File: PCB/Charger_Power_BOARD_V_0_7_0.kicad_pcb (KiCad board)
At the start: 4 copper layers, 208 x 117.5 mm, 333 parts, among them IC10 TLA431AIDBZR, IC15 VO618A-3X017T, IC16 LM4040C30FTA, IC17 MCP6541RT-I_OT, IC18 VO618A-3X017T, IC19 TPS54302DDCT, IC20 74LVC1G17GW,125, IC21 VO618A-3X017T, IC22 LM4040C30FTA, IC23 MCP6541RT-I_OT, IC24 VO618A-3X017T, IC25 74LVC1G17GW,125, IC26 VO618A-3X017T, IC27 LM4040C30FTA, IC28 LM75BD,118, IC45 MCP6541RT-I_OT, IC46 VO618A-3X017T, IC47 74LVC1G17GW,125, IC48 VO618A-3X017T, IC49 LM4040C30FTA, IC50 MCP6541RT-I_OT, IC51 VO618A-3X017T, IC52 74LVC1G17GW,125, IC9 STM32C031C6T6, J1 AMT0440005TH0000G, J10 AMT0440005TH0000G, J11 AMT0440005TH0000G, J12 AMT0440005TH0000G, J13 AMT0440005TH0000G, J14 AMT0440005TH0000G, J15 AMT0440005TH0000G, J18 Conn_01x03_Pin, J19 Screw_Terminal_01x02, J2 Conn_01x05_Socket, J20 Screw_Terminal_01x02, J3 AMT0440005TH0000G, J4 Conn_01x04_Socket, J5 AMT0440005TH0000G, J6 B6B-XH-A_LF__SN_, J7 AMT0440005TH0000G, J8 Conn_01x02_Socket, J9 B6B-XH-A_LF__SN_, K5 Relay_IM_NE801A, K6 Relay_IM_NE801A, Q10 DMN60H080DS, Q5 BSS316N H6327, Q6 BSS316N H6327, Q7 DMN60H080DS, Q8 DMN60H080DS, Q9 DMN60H080DS, SW1 SW_SPST, SW2 SW_SPST, T11 ZMPT101B, T7 ZMPT101B, T9 ZMPT101B, U1 THVD1400DR, U10 IVY-CT-PCB-01-10A, U11 DRV8220DRL, U12 IVY-CT-PCB-01-10A, U13 IVY-CT-PCB-01-10A, U4 TLV1805DBVR, U5 TLV1805DBVR, U6 ADE7953xCP, U7 ADE7953xCP, U8 RCD MD0630STA-P, U9 ADE7953xCP, Y3 CX2016FB48000C0FZZH1, Y4 GC0350016, Y5 GC0350016, Y6 GC0350016

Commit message: continuação do layout
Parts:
- moved C29 125.5 mm to (112.2, -16.5)
- moved C30 125.5 mm to (112.2, -14.0)
- moved IC20 125.5 mm to (122.9, -34.3)
- moved R74 125.5 mm to (120.2, -21.5)
- moved R75 125.5 mm to (120.2, -19.0)
- moved D28 102.1 mm to (201.5, 38.0)
- moved R73 95.9 mm to (187.8, 31.5), turned to 180 degrees
- moved R49 95.8 mm to (187.8, 34.0), turned to 180 degrees
- moved C25 92.8 mm to (190.2, 34.5), turned to -90 degrees
- moved R50 89.3 mm to (197.0, 34.5), turned to 90 degrees
- moved C27 86.8 mm to (198.5, 34.5), turned to 90 degrees
- moved IC16 86.7 mm to (193.2, 34.5)
- moved IC17 86.6 mm to (193.2, 29.5)
- moved R66 84.6 mm to (204.5, 35.5)
- moved R70 84.4 mm to (190.2, 29.5), turned to -90 degrees
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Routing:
- net -12V: track 50.6 -> 57.8 mm, vias 4 -> 5
- net +3V3: track 89.0 -> 81.8 mm, vias 27 -> 26
- net /UART0_RX: track 75.3 -> 72.4 mm, vias 2 -> 1
- net /UART0_TX: track 75.5 -> 74.2 mm, vias 2 -> 1
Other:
- outline, holes or cut-outs redrawn

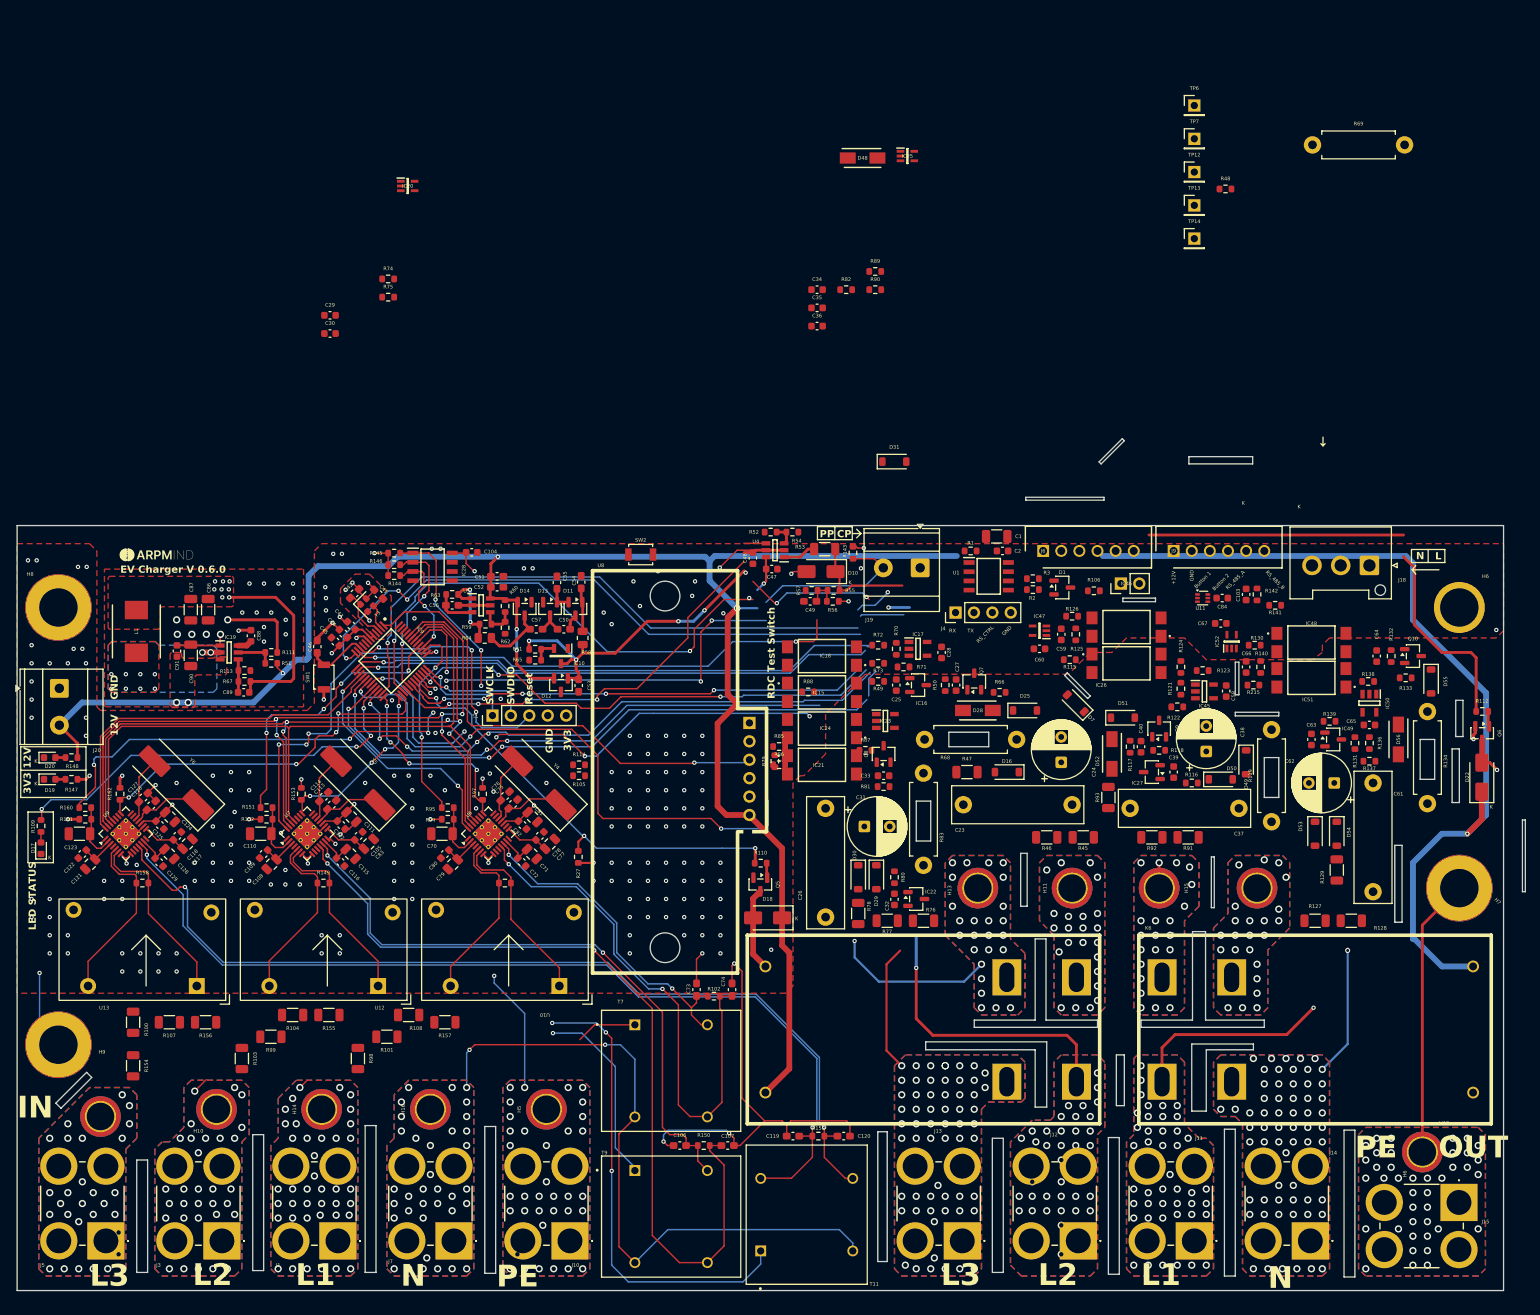
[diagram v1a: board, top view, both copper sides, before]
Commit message: Routing terminado; A corrigir violações; falta colocar as proteçãoes de inversão de polaridade; fusivél; TVS
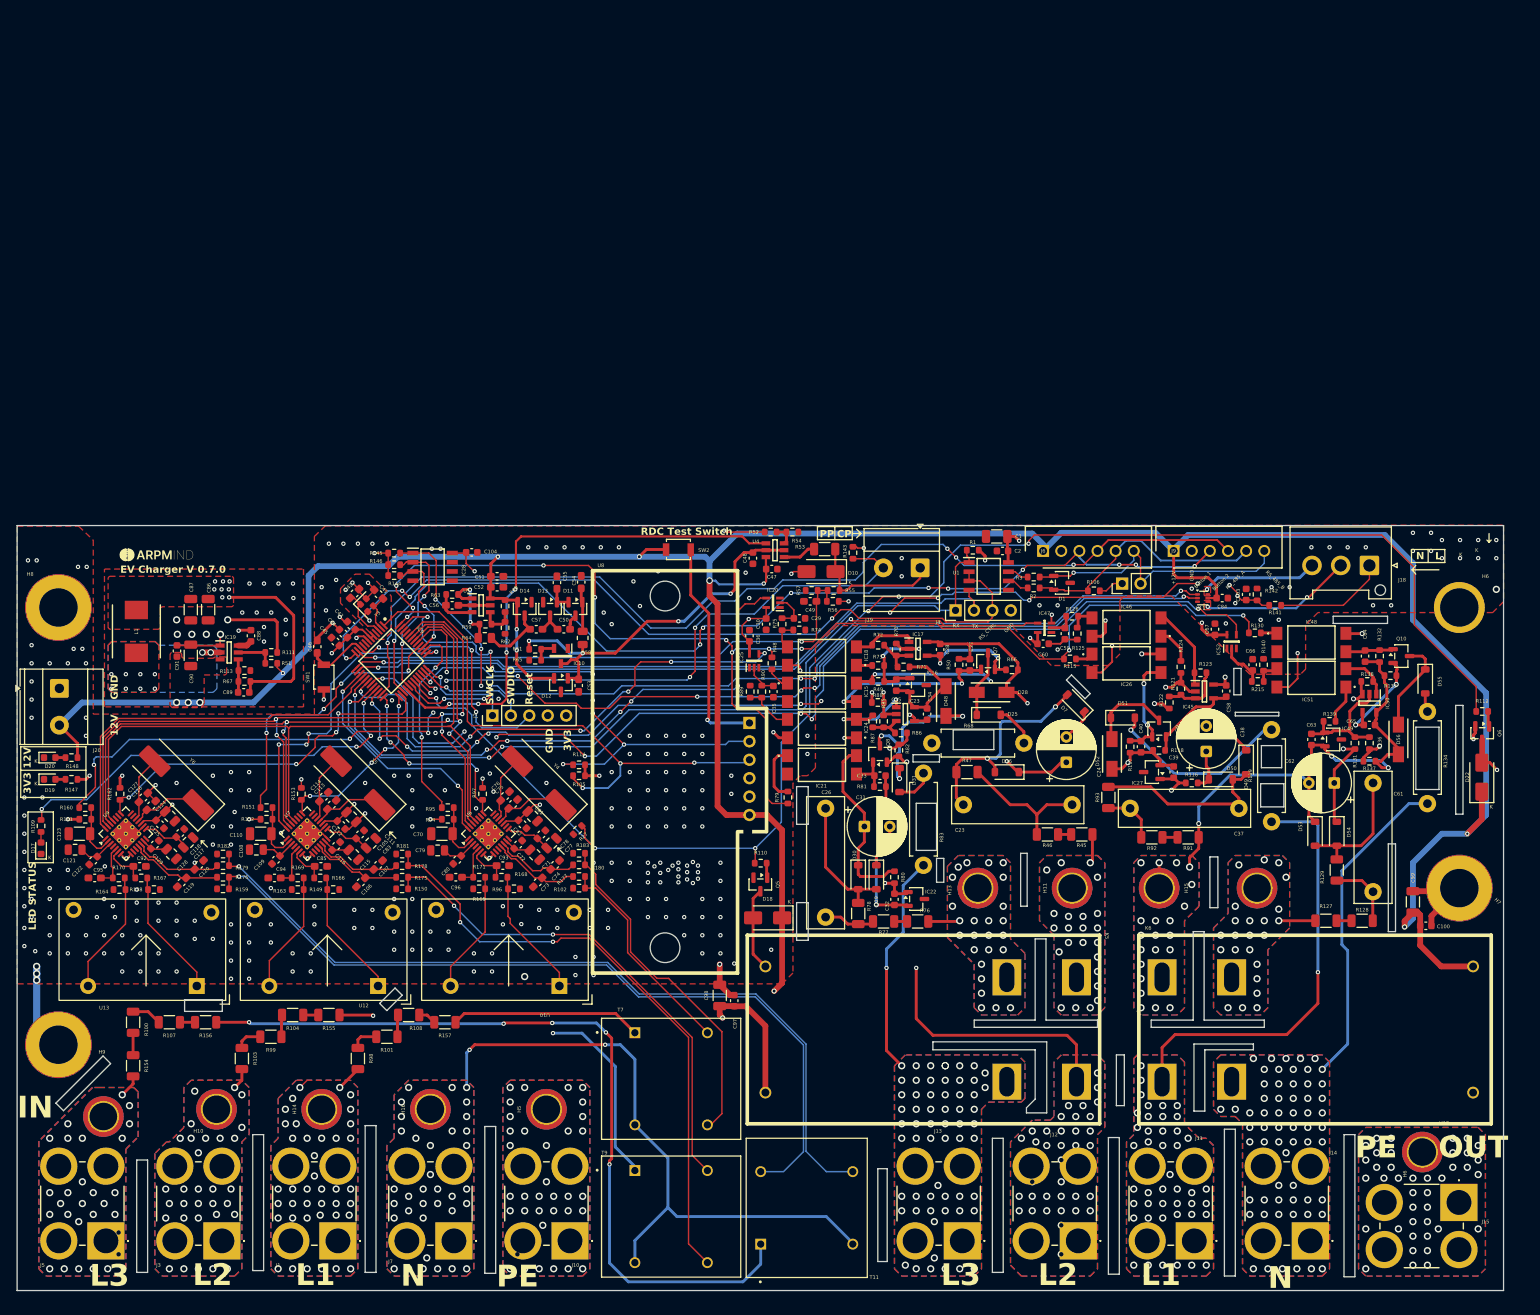
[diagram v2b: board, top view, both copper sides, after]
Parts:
- removed R69: 22K, Resistor_THT:R_Axial_DIN0411_L9.9mm_D3.6mm_P12.70mm_Horizontal
- removed TP12, TP13, TP14, TP6, TP7: TestPoint, Connector_PinHeader_2.54mm:PinHeader_1x01_P2.54mm_Vertical
- added C100: 0.1uF, Capacitor_SMD:C_0603_1608Metric, F.Cu at (263.3, 67.7)
- added C85: 33nF, Capacitor_SMD:C_0603_1608Metric_Pad1.08x0.95mm_HandSolder, F.Cu at (110.9, 59.5)
- added C92: 33nF, Capacitor_SMD:C_0603_1608Metric_Pad1.08x0.95mm_HandSolder, F.Cu at (85.9, 59.5)
- added C93: 33nF, Capacitor_SMD:C_0603_1608Metric_Pad1.08x0.95mm_HandSolder, F.Cu at (136.0, 59.4)
- added C94: 33nF, Capacitor_SMD:C_0603_1608Metric_Pad1.08x0.95mm_HandSolder, F.Cu at (104.5, 61.1)
- added C95: 33nF, Capacitor_SMD:C_0603_1608Metric_Pad1.08x0.95mm_HandSolder, F.Cu at (79.7, 61.1)
- added C96: 33nF, Capacitor_SMD:C_0603_1608Metric_Pad1.08x0.95mm_HandSolder, F.Cu at (129.5, 61.0)
- added C97: 0.1uF, Capacitor_SMD:C_0603_1608Metric, F.Cu at (167.9, 78.0)
- added C98: 10uF, Capacitor_SMD:C_1206_3216Metric, F.Cu at (165.9, 77.3)
- added C99: 10uF, Capacitor_SMD:C_1206_3216Metric, F.Cu at (261.5, 64.4)
- added R163: 4R99, Resistor_SMD:R_0603_1608Metric, F.Cu at (107.7, 62.7)
- added R164: 4R99, Resistor_SMD:R_0603_1608Metric, F.Cu at (83.1, 62.7)
- added R165: 4R99, Resistor_SMD:R_0603_1608Metric, F.Cu at (132.7, 62.6)
- added R166: 1K, Resistor_SMD:R_0603_1608Metric, F.Cu at (110.8, 61.1)
- added R167: 1K, Resistor_SMD:R_0603_1608Metric, F.Cu at (86.1, 61.1)
- added R168: 1K, Resistor_SMD:R_0603_1608Metric, F.Cu at (135.8, 61.0)
- added R169: 1K, Resistor_SMD:R_0603_1608Metric, F.Cu at (107.7, 61.1)
- added R170: 1K, Resistor_SMD:R_0603_1608Metric, F.Cu at (83.0, 61.1)
- added R171: 1K, Resistor_SMD:R_0603_1608Metric, F.Cu at (132.7, 61.0)
- added R175: 1K, Resistor_SMD:R_0603_1608Metric, F.Cu at (122.1, 61.0)
- added R176: 1K, Resistor_SMD:R_0603_1608Metric, F.Cu at (97.4, 61.0)
- added R177: 1K, Resistor_SMD:R_0603_1608Metric, F.Cu at (146.5, 60.9)
- added R178: 1K, Resistor_SMD:R_0603_1608Metric, F.Cu at (122.1, 59.4)
- added R179: 1K, Resistor_SMD:R_0603_1608Metric, F.Cu at (97.4, 59.4)
- added R180: 1K, Resistor_SMD:R_0603_1608Metric, F.Cu at (146.5, 59.3)
- added R181: 49R9, Resistor_SMD:R_0603_1608Metric, F.Cu at (122.1, 57.8)
- added R182: 49R9, Resistor_SMD:R_0603_1608Metric, F.Cu at (97.4, 57.8)
- added R183: 49R9, Resistor_SMD:R_0603_1608Metric, F.Cu at (146.5, 57.7)
- C110, C123, C70: value 10uF -> 1uF
- R102, R150, R159: value 100R -> 49R9
- R110, R112: value 100R -> 470R
- R149, R158, R96: value 15R8 -> 4R99
- moved C120 96.4 mm to (94.1, 59.3), turned to -135 degrees
- moved C119 91.3 mm to (91.7, 61.7), turned to -135 degrees
- moved R48 90.5 mm to (173.1, 31.5), turned to 90 degrees
- moved R159 88.9 mm to (97.4, 62.6), turned to 180 degrees
- moved C29 77.1 mm to (176.9, 25.3)
- moved IC20 76.4 mm to (173.2, 23.1), turned to 180 degrees
- moved D48 75.8 mm to (197.1, 36.7), turned to 90 degrees
- moved R74 74.6 mm to (176.9, 26.9), turned to 180 degrees
- moved IC25 72.7 mm to (170.7, 31.1), turned to 90 degrees
- moved C30 72.3 mm to (172.3, 26.1), turned to -90 degrees
- moved R75 70.6 mm to (174.5, 26.1), turned to -90 degrees
- moved R82 63.9 mm to (190.6, 43.5), turned to 90 degrees
- moved C107 61.8 mm to (118.8, 59.3), turned to -135 degrees
- moved C34 60.5 mm to (194.5, 38.5), turned to 90 degrees
- moved R89 60.5 mm to (170.1, 35.4), turned to -90 degrees
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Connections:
- C106 pad 1: GND -> Net-(U7-VN)
- C106 pad 2: Net-(U7-VP) -> GND
- C107 pad 2: Net-(U7-VN) -> Net-(U7-VP)
- C119 pad 1: GND -> Net-(U9-VN)
- C119 pad 2: Net-(U9-VP) -> GND
- C120 pad 2: Net-(U9-VN) -> Net-(U9-VP)
- C24 pad 2: /Welding_Contact_Detector1/Neutral_RelayIN -> /Neutral_RelayIN
- C25 pad 2: /Welding_Contact_Detector1/Neutral_RelayIN -> /Neutral_RelayIN
- C27 pad 2: /Welding_Contact_Detector1/Neutral_RelayIN -> /Neutral_RelayIN
- C28 pad 2: /Welding_Contact_Detector1/Neutral_RelayIN -> /Neutral_RelayIN
- C73 pad 1: GND -> Net-(U6-VN)
- C73 pad 2: Net-(U6-VP) -> GND
- C74 pad 2: Net-(U6-VN) -> Net-(U6-VP)
- D28 pad 2: /Welding_Contact_Detector1/Neutral_RelayIN -> /Neutral_RelayIN
- D7 pad 1: /Welding_Contact_Detector1/Neutral_RelayIN -> /Neutral_RelayIN
- IC16 pad 2: /Welding_Contact_Detector1/Neutral_RelayIN -> /Neutral_RelayIN
- IC17 pad 5: /Welding_Contact_Detector1/Neutral_RelayIN -> /Neutral_RelayIN
- IC9 pad 47: unconnected-(IC9-PB8-Pad47) -> /RDC_TEST
- R102 pad 1: Net-(U6-VP) -> Net-(R102-Pad1)
- R102 pad 2: Net-(U6-VN) -> GND
- R149 pad 1: Net-(U7-IAP) -> GND
- R149 pad 2: Net-(U7-IAN) -> Net-(R149-Pad2)
- R150 pad 1: Net-(U7-VP) -> Net-(R150-Pad1)
- R150 pad 2: Net-(U7-VN) -> GND
- R158 pad 1: Net-(U9-IAP) -> GND
- R158 pad 2: Net-(U9-IAN) -> Net-(R158-Pad2)
- R159 pad 1: Net-(U9-VP) -> Net-(R159-Pad1)
- R159 pad 2: Net-(U9-VN) -> GND
- R50 pad 2: /Welding_Contact_Detector1/Neutral_RelayIN -> /Neutral_RelayIN
- R66 pad 2: /Welding_Contact_Detector1/Neutral_RelayIN -> /Neutral_RelayIN
- R71 pad 2: /Welding_Contact_Detector1/Neutral_RelayIN -> /Neutral_RelayIN
- R96 pad 1: Net-(U6-IAP) -> GND
- R96 pad 2: Net-(U6-IAN) -> Net-(R168-Pad2)
- T11 pad 3: Net-(U9-VN) -> Net-(R179-Pad1)
- T11 pad 4: Net-(U9-VP) -> Net-(R159-Pad1)
- T7 pad 3: Net-(U6-VN) -> Net-(R180-Pad1)
- T7 pad 4: Net-(U6-VP) -> Net-(R102-Pad1)
- T9 pad 3: Net-(U7-VN) -> Net-(R178-Pad1)
- T9 pad 4: Net-(U7-VP) -> Net-(R150-Pad1)
- U10 pad 1: Net-(U6-IAN) -> Net-(R168-Pad2)
- U10 pad 2: Net-(U6-IAP) -> Net-(R165-Pad1)
- U12 pad 1: Net-(U7-IAN) -> Net-(R149-Pad2)
- U12 pad 2: Net-(U7-IAP) -> Net-(R163-Pad1)
- U13 pad 1: Net-(U9-IAN) -> Net-(R158-Pad2)
- U13 pad 2: Net-(U9-IAP) -> Net-(R164-Pad1)
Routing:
- net /Neutral_RelayIN: track 0.14 -> 205.7 mm, vias 23 -> 32
- net /EN_WEL_Detec: track 0.00 -> 175.6 mm, vias 0 -> 11
- net Net-(U9-VP): track 132.7 -> 12.5 mm, vias 2 -> 0
- net Net-(U9-VN): track 131.1 -> 13.0 mm, vias 2 -> 0
- net Net-(R179-Pad1): track 0.00 -> 113.8 mm, vias 0 -> 1
- net Net-(R159-Pad1): track 0.00 -> 112.2 mm, vias 0 -> 1
- net Net-(U7-VN): track 118.3 -> 12.6 mm, vias 2 -> 0
- net Net-(R178-Pad1): track 0.00 -> 84.5 mm, vias 0 -> 2
- net /RDC_TEST: track 0.75 -> 75.9 mm, vias 0 -> 8
- net Net-(U7-VP): track 86.3 -> 12.2 mm, vias 2 -> 0
- net /Line1_RelayIN: track 3.60 -> 76.0 mm, vias 21 -> 24
- net Net-(R150-Pad1): track 0.00 -> 69.2 mm, vias 0 -> 2
- net /CABLE_lock: track 81.0 -> 147.2 mm, vias 5 -> 13
- net Net-(U6-VN): track 74.5 -> 12.4 mm, vias 2 -> 0
- net +12V: track 386.6 -> 448.6 mm, vias 9 -> 14
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- added copper zone on F.Cu, net Net-(J18-Pin_2)
- added copper zone on F.Cu, net Net-(J18-Pin_3)
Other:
- board size 208 x 117.5 mm -> 205 x 105.5 mm
- board text added: "EV Charger V 0.7.0"
- board text removed: "EV Charger V 0.6.0"

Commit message: Layout finalizado
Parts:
- removed SW2: SW_SPST, Button_Switch_SMD:SW_SPST_B3U-1000P
- added D2: BZT52C13, Diode_SMD:D_SOD-123, F.Cu at (100.1, 38.0)
- added D3: SMBJ14A, FOOTPRINTS:DIOM5436X261N, F.Cu at (101.5, 34.5)
- added F1: SF-3812TL400T-2, FOOTPRINTS:SF3812TL400T2, F.Cu at (76.9, 35.2)
- added Q1: BSS84, Package_TO_SOT_SMD:SOT-23, F.Cu at (163.4, 15.9)
- added Q11: BSS316N H6327, Package_TO_SOT_SMD:SOT-23, F.Cu at (156.7, 15.9)
- added Q2: SQD50P04-13L_T4GE3, FOOTPRINTS:SQD50P0413L_T4GE3, F.Cu at (90.7, 36.1)
- added R120: 470R, Resistor_SMD:R_0603_1608Metric, F.Cu at (151.8, 16.7)
- added R172: 10K, Resistor_SMD:R_0603_1608Metric, F.Cu at (99.3, 40.4)
- added R173: 120R, Resistor_SMD:R_0603_1608Metric, F.Cu at (166.0, 15.9)
- added R28: 10K, Resistor_SMD:R_0603_1608Metric, F.Cu at (154.1, 16.0)
- added R69: 100K, Resistor_SMD:R_0603_1608Metric, F.Cu at (160.9, 16.1)
- added R84: 100K, Resistor_SMD:R_0603_1608Metric, F.Cu at (159.3, 16.1)
- H9: footprint MountingHole:MountingHole_5.3mm_M5_DIN965_Pad_TopBottom -> MountingHole:MountingHole_5.3mm_M5
- moved D19 79.4 mm to (145.5, 14.0)
- moved R147 79.4 mm to (148.5, 14.0)
- moved D20 70.0 mm to (136.5, 14.0)
- moved R148 70.0 mm to (139.5, 14.0)
- moved G*** 13.7 mm to (74.9, 14.1)
- moved C24 8.38 mm to (213.1, 36.8), turned to 180 degrees
- moved D7 7.05 mm to (214.2, 44.0), turned to 90 degrees
- moved J20 6.50 mm to (74.7, 41.5)
- moved C86 5.91 mm to (95.3, 18.2)
- moved C87 5.91 mm to (93.0, 18.2)
- moved C89 5.91 mm to (100.2, 29.6)
- moved C91 5.91 mm to (91.0, 23.9)
- moved IC19 5.91 mm to (98.2, 24.1)
- moved L1 5.91 mm to (85.5, 21.2)
- moved R111 5.91 mm to (104.0, 24.1)
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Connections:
- IC9 pad 46: unconnected-(IC9-PB7-Pad46) -> /RCD_TEST_DRIVE
- J20 pad 1: GND -> +12V_EXT
- J20 pad 2: +12V -> GND
- U6 pad 10: /Power_Phase/IBN -> GND
- U6 pad 9: /Power_Phase/IBP -> GND
- U7 pad 10: /Power_Phase1/IBN -> GND
- U7 pad 9: /Power_Phase1/IBP -> GND
- U9 pad 10: /Power_Phase2/IBN -> GND
- U9 pad 9: /Power_Phase2/IBP -> GND
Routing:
- net /RCD_TEST_DRIVE: track 0.00 -> 37.4 mm, vias 0 -> 4
- net +12V: track 448.6 -> 430.2 mm, vias 14 -> 16
- net /Neutral_RelayIN: track 205.7 -> 215.5 mm, vias 32 -> 28
- net Net-(D2-A): track 0.00 -> 9.11 mm
- net GND: track 218.7 -> 227.2 mm, vias 395 -> 424
- net Net-(D18-A): track 11.5 -> 17.6 mm
- net Net-(R156-Pad1): track 112.3 -> 117.3 mm, vias 5 -> 3
- net Net-(D16-A): track 30.0 -> 33.9 mm
- net Net-(IC45-OUT): track 11.5 -> 15.2 mm, vias 0 -> 2
- net Net-(Q1-G): track 0.00 -> 3.19 mm
- net /Welding_Contact_Detector1/+5V_n: track 41.1 -> 44.3 mm
- net Net-(Q11-G): track 0.00 -> 3.18 mm
- net /SPI_MISO: track 112.3 -> 109.4 mm
- net Net-(R108-Pad1): track 2.49 -> 5.31 mm
- net /SPI_SCK: track 106.7 -> 103.9 mm
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- added copper zone on F.Cu, net +12V_EXT
- added copper zone on F.Cu, net Net-(Q2-D)
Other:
- outline, holes or cut-outs redrawn
- board text added: "ARPM_CHARGER_01_V0_7_0"
- board text removed: "L"
- board text removed: "RDC Test Switch"
